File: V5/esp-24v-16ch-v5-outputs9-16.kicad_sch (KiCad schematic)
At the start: 5 parts, among them Q12 MMBT2222A

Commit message: Created V5
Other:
- title: ESP 24V 16xIn/16xOut/4xNTC Module -> ESP 24V 16xIn/16xOut/1-Wire Module
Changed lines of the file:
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@@
 	(paper "A4")
 	(title_block
-		(title "ESP 24V 16xIn/16xOut/4xNTC Module")
-		(date "2025-07-04")
-		(rev "V4.1")
+		(title "ESP 24V 16xIn/16xOut/1-Wire Module")
+		(date "2025-12-09")
+		(rev "V5")
 	)
 	(text "I_{LED} = (24V - V_{LED}) / 6.8k\nI_{LED} = (24V - 2.7V) / 6.8k\nI_{LED} = 3,13 mA"
@@
 		)
 		(instances
-			(project "esp-24v-16ch-v4"
+			(project "esp-24v-16ch-v5"
 				(path "/2bc5a21a-1d79-419d-a592-6852cc07b00a/118d8d95-c0ce-4d84-8406-4e7809444f6f"
 					(reference "#PWR0141")
@@
 		)
 		(instances
-			(project "esp-24v-16ch-v4"
+			(project "esp-24v-16ch-v5"
 				(path "/2bc5a21a-1d79-419d-a592-6852cc07b00a/118d8d95-c0ce-4d84-8406-4e7809444f6f"
 					(reference "Q13")
@@
 		)
 		(instances
-			(project "esp-24v-16ch-v4"
+			(project "esp-24v-16ch-v5"
 				(path "/2bc5a21a-1d79-419d-a592-6852cc07b00a/118d8d95-c0ce-4d84-8406-4e7809444f6f"
 					(reference "#PWR0142")
@@
 		)
 		(instances
-			(project "esp-24v-16ch-v4"
+			(project "esp-24v-16ch-v5"
 				(path "/2bc5a21a-1d79-419d-a592-6852cc07b00a/118d8d95-c0ce-4d84-8406-4e7809444f6f"
 					(reference "R116")
@@
 		)
 		(instances
-			(project "esp-24v-16ch-v4"
+			(project "esp-24v-16ch-v5"
 				(path "/2bc5a21a-1d79-419d-a592-6852cc07b00a/118d8d95-c0ce-4d84-8406-4e7809444f6f"
 					(reference "#PWR0140")
@@
 		)
 		(instances
-			(project "esp-24v-16ch-v4"
+			(project "esp-24v-16ch-v5"
 				(path "/2bc5a21a-1d79-419d-a592-6852cc07b00a/118d8d95-c0ce-4d84-8406-4e7809444f6f"
 					(reference "R115")
@@
 		)
 		(instances
-			(project "esp-24v-16ch-v4"
+			(project "esp-24v-16ch-v5"
 				(path "/2bc5a21a-1d79-419d-a592-6852cc07b00a/118d8d95-c0ce-4d84-8406-4e7809444f6f"
 					(reference "D66")
@@
 		)
 		(instances
-			(project "esp-24v-16ch-v4"
+			(project "esp-24v-16ch-v5"
 				(path "/2bc5a21a-1d79-419d-a592-6852cc07b00a/118d8d95-c0ce-4d84-8406-4e7809444f6f"
 					(reference "R117")

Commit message: Updates and corrections to SCH and PCB
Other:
- note added: "I_{LED} = (24V - V_{LED} - V_{CE}) / 10k I_{LED} = (24V - 2.7V - 0,1V) / 10k I_{LED} = 2,12 mA"
- note removed: "I_{LED} = (24V - V_{LED}) / 6.8k I_{LED} = (24V - 2.7V) / 6.8k I_{LED} = 3,13 mA"
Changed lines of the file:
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@@
 		(rev "V5")
 	)
-	(text "I_{LED} = (24V - V_{LED}) / 6.8k\nI_{LED} = (24V - 2.7V) / 6.8k\nI_{LED} = 3,13 mA"
+	(text "I_{LED} = (24V - V_{LED} - V_{CE}) / 10k\nI_{LED} = (24V - 2.7V - 0,1V) / 10k\nI_{LED} = 2,12 mA"
 		(exclude_from_sim no)
 		(at 154.94 86.36 0)

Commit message: Many changes!
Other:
- note added: "RESISTORS: 62,5mW WHERE NOT SPECIFIED"
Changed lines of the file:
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@@
 		(rev "V5.1")
+	)
+	(text "RESISTORS: 62,5mW WHERE NOT SPECIFIED"
+		(exclude_from_sim no)
+		(at 182.88 171.45 0)
+		(effects
+			(font
+				(size 1.905 1.905)
+			)
+			(justify left)
+		)
 	)
 	(text "I_{LED} = (24V - V_{LED} - V_{CE}) / 10k\nI_{LED} = (24V - 2.7V - 0,1V) / 10k\nI_{LED} = 2,12 mA"

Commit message: Reviewed capacitor sizes and voltages.
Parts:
- R112: Package 0402/1005 -> (none)
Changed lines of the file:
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@@
 			)
 		)
-		(property "Package" "0402/1005"
+		(property "Package" ""
 			(at 101.6 106.68 0)
 			(effects

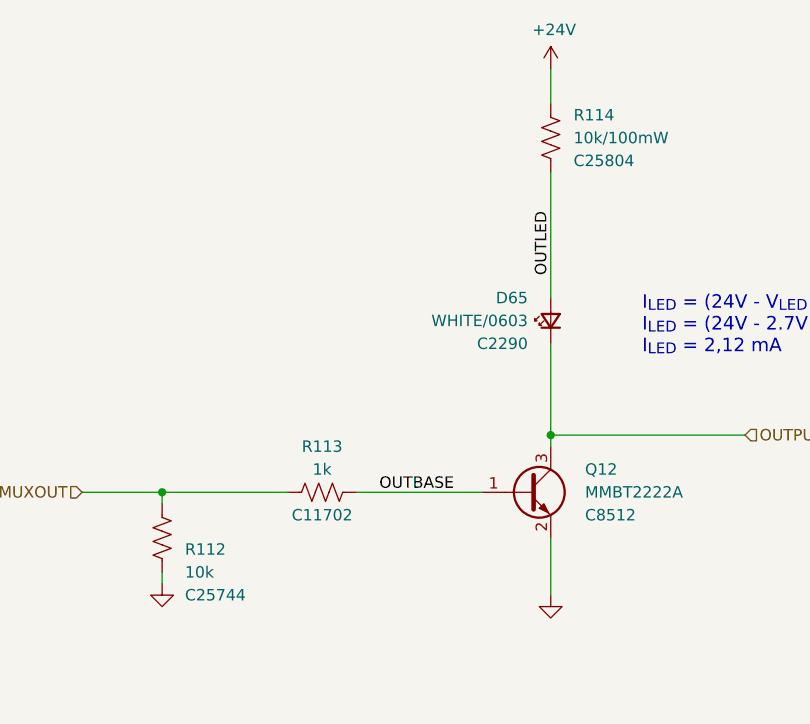
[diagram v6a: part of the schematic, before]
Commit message: Inputs GND separated from main GND.
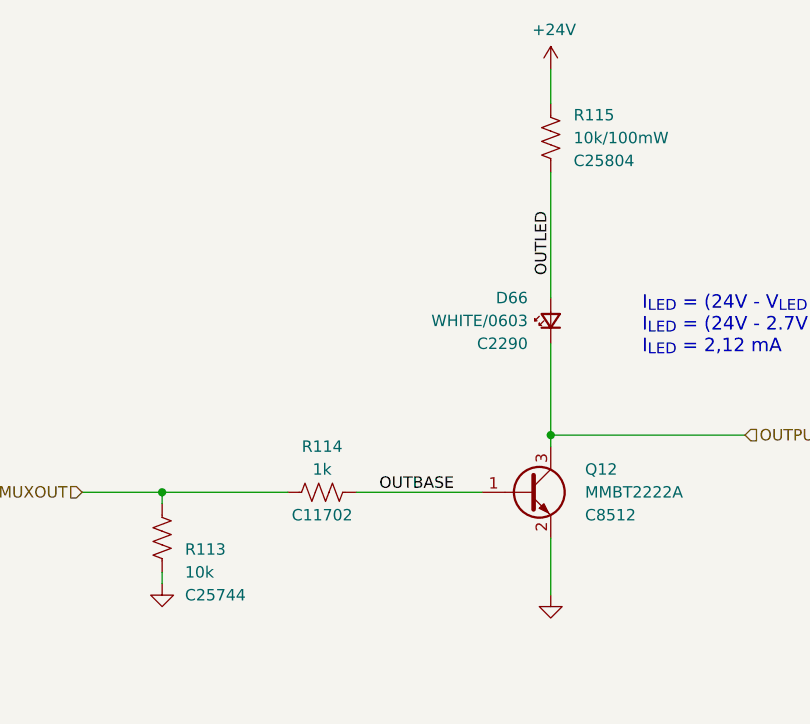
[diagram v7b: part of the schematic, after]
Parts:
- renumbered D65 to D66, R112 to R113, R113 to R114, R114 to R115
